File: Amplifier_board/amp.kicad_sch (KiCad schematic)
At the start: 24 parts, among them U1 TPA3111D1PWPR

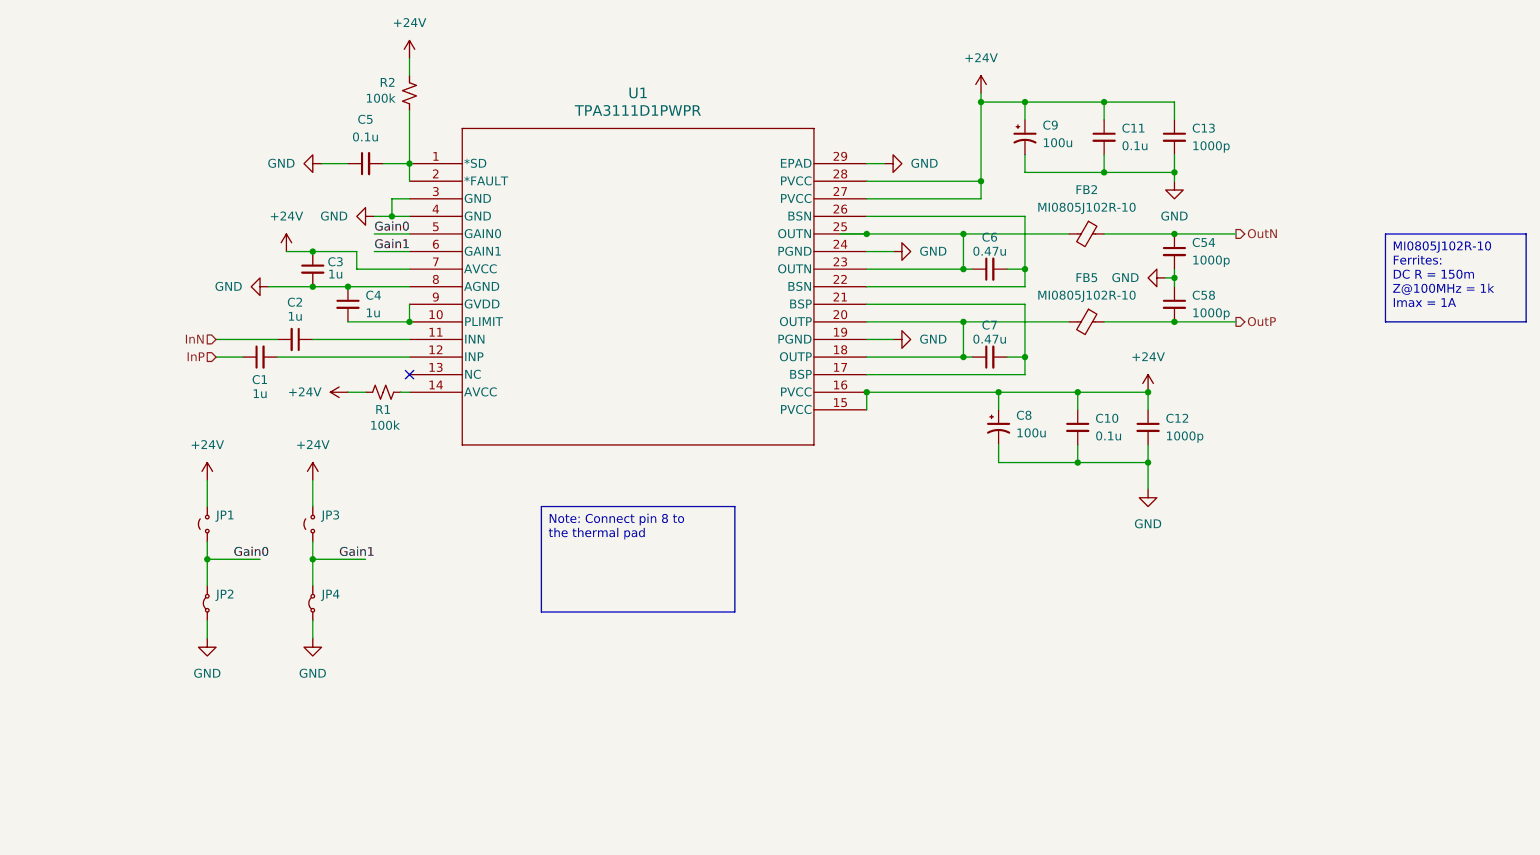
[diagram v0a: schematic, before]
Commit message: Added buffers at DAC outputs
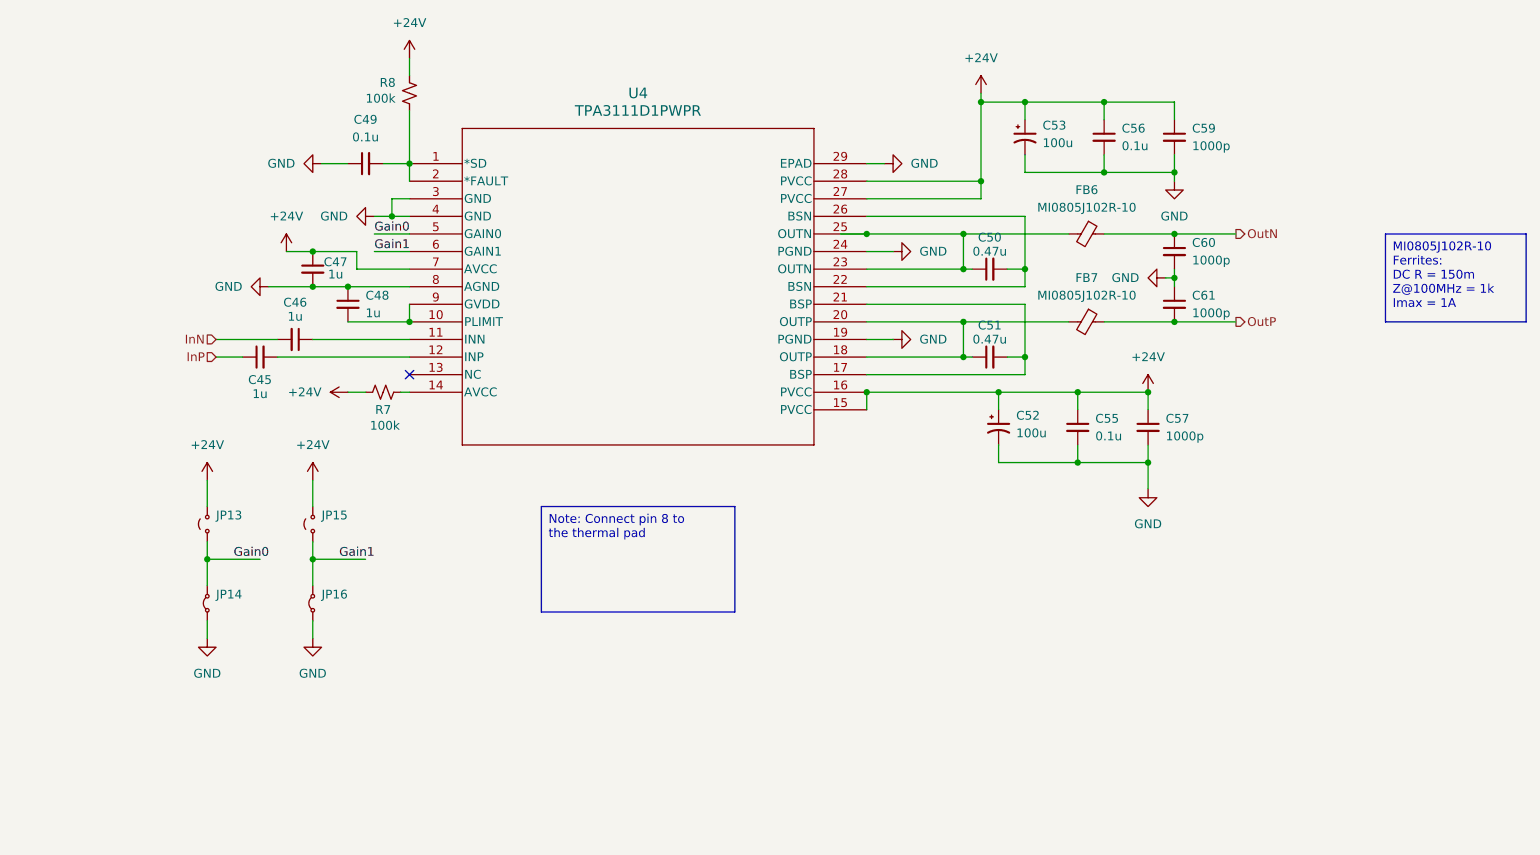
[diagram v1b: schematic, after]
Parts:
- renumbered C1 to C45, C2 to C46, C3 to C47, C4 to C48, C5 to C49, C6 to C50, C7 to C51, C8 to C52, C9 to C53, C10 to C55, C11 to C56, C12 to C57, C13 to C59, C54 to C60, C58 to C61, FB2 to FB6, FB5 to FB7, JP1 to JP13, JP2 to JP14, JP3 to JP15, JP4 to JP16, R1 to R7, R2 to R8, U1 to U4
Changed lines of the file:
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@@
 		(dnp no)
 		(fields_autoplaced yes)
-		(property "Reference" "C4"
+		(property "Reference" "C48"
 			(at 96.52 82.5562 0)
 			(effects
@@
 		(on_board yes)
 		(dnp no)
-		(property "Reference" "C6"
+		(property "Reference" "C50"
 			(at 186.69 74.168 90)
 			(effects
@@
 		(on_board yes)
 		(dnp no)
-		(property "Reference" "R2"
+		(property "Reference" "R8"
 			(at 98.552 51.816 0)
 			(effects
@@
 		(on_board yes)
 		(dnp no)
-		(property "Reference" "C3"
+		(property "Reference" "C47"
 			(at 92.202 77.724 0)
 			(effects
@@
 		(dnp no)
 		(fields_autoplaced yes)
-		(property "Reference" "JP2"
+		(property "Reference" "JP14"
 			(at 74.93 125.7299 90)
 			(effects
@@
 		(dnp no)
 		(fields_autoplaced yes)
-		(property "Reference" "#PWR016"
+		(property "Reference" "#PWR072"
 			(at 209.55 116.84 0)
 			(effects
@@
 		(dnp no)
 		(fields_autoplaced yes)
-		(property "Reference" "#PWR05"
+		(property "Reference" "#PWR060"
 			(at 88.9 113.03 0)
 			(effects
@@
 		(dnp no)
 		(fields_autoplaced yes)
-		(property "Reference" "#PWR015"
+		(property "Reference" "#PWR070"
 			(at 209.55 100.33 0)
 			(effects
@@
 		(dnp no)
 		(fields_autoplaced yes)
-		(property "Reference" "C5"
+		(property "Reference" "C49"
 			(at 96.5263 57.15 90)
 			(effects
@@
 		(dnp no)
 		(fields_autoplaced yes)
-		(property "Reference" "C10"
+		(property "Reference" "C55"
 			(at 201.93 100.3362 0)
 			(effects
@@
 		(dnp no)
 		(fields_autoplaced yes)
-		(property "Reference" "C8"
+		(property "Reference" "C52"
 			(at 190.5 99.8981 0)
 			(effects
@@
 		(dnp no)
 		(fields_autoplaced yes)
-		(property "Reference" "FB2"
+		(property "Reference" "FB6"
 			(at 200.6981 67.31 90)
 			(effects
@@
 					(unit 1)
 				)
+				(path "/991395a4-3885-4774-b551-0bfe029123d3/26541e86-2f42-461f-bb67-92277cc28a80"
+					(reference "FB?")
+					(unit 1)
+				)
 				(path "/991395a4-3885-4774-b551-0bfe029123d3/e8898fe0-55dc-4973-83e9-f265cc01a132"
 					(reference "FB1")
@@
 		(dnp no)
 		(fields_autoplaced yes)
-		(property "Reference" "#PWR02"
+		(property "Reference" "#PWR057"
 			(at 73.66 138.43 0)
 			(effects
@@
 		(dnp no)
 		(fields_autoplaced yes)
-		(property "Reference" "#PWR07"
+		(property "Reference" "#PWR062"
 			(at 83.82 63.5 0)
 			(effects
@@
 		(dnp no)
 		(fields_autoplaced yes)
-		(property "Reference" "C9"
+		(property "Reference" "C53"
 			(at 194.31 57.9881 0)
 			(effects
@@
 		(dnp no)
 		(fields_autoplaced yes)
-		(property "Reference" "JP3"
+		(property "Reference" "JP15"
 			(at 90.17 114.2999 90)
 			(effects
@@
 		(dnp no)
 		(fields_autoplaced yes)
-		(property "Reference" "C13"
+		(property "Reference" "C59"
 			(at 215.9 58.4262 0)
 			(effects
@@
 		(on_board yes)
 		(dnp no)
-		(property "Reference" "C54"
+		(property "Reference" "C60"
 			(at 215.9 74.9362 0)
 			(effects
@@
 		(dnp no)
 		(fields_autoplaced yes)
-		(property "Reference" "U1"
+		(property "Reference" "U4"
 			(at 135.89 53.34 0)
 			(effects
@@
 		(dnp no)
 		(fields_autoplaced yes)
-		(property "Reference" "#PWR03"
+		(property "Reference" "#PWR058"
 			(at 76.2 81.28 0)
 			(effects
@@
 		(dnp no)
 		(fields_autoplaced yes)
-		(property "Reference" "#PWR011"
+		(property "Reference" "#PWR066"
 			(at 177.8 63.5 0)
 			(effects
@@
 		(dnp no)
 		(fields_autoplaced yes)
-		(property "Reference" "C12"
+		(property "Reference" "C57"
 			(at 212.09 100.3362 0)
 			(effects
@@
 		(dnp no)
 		(fields_autoplaced yes)
-		(property "Reference" "#PWR014"
+		(property "Reference" "#PWR069"
 			(at 185.42 57.15 0)
 			(effects
@@
 		(dnp no)
 		(fields_autoplaced yes)
-		(property "Reference" "#PWR017"
+		(property "Reference" "#PWR074"
 			(at 213.36 72.39 0)
 			(effects
@@
 		(dnp no)
 		(fields_autoplaced yes)
-		(property "Reference" "#PWR08"
+		(property "Reference" "#PWR063"
 			(at 97.79 96.52 0)
 			(effects
@@
 		(dnp no)
 		(fields_autoplaced yes)
-		(property "Reference" "#PWR01"
+		(property "Reference" "#PWR056"
 			(at 73.66 113.03 0)
 			(effects
@@
 		(on_board yes)
 		(dnp no)
-		(property "Reference" "R1"
+		(property "Reference" "R7"
 			(at 99.06 99.06 90)
 			(effects
@@
 		(dnp no)
 		(fields_autoplaced yes)
-		(property "Reference" "#PWR010"
+		(property "Reference" "#PWR065"
 			(at 102.87 52.07 0)
 			(effects
@@
 		(dnp no)
 		(fields_autoplaced yes)
-		(property "Reference" "#PWR071"
+		(property "Reference" "#PWR073"
 			(at 205.74 80.01 0)
 			(effects
@@
 		(dnp no)
 		(fields_autoplaced yes)
-		(property "Reference" "C11"
+		(property "Reference" "C56"
 			(at 205.74 58.4262 0)
 			(effects
@@
 		(dnp no)
 		(fields_autoplaced yes)
-		(property "Reference" "FB5"
+		(property "Reference" "FB7"
 			(at 200.6981 80.01 90)
 			(effects
@@
 		(dnp no)
 		(fields_autoplaced yes)
-		(property "Reference" "#PWR013"
+		(property "Reference" "#PWR068"
 			(at 179.07 88.9 0)
 			(effects
@@
 		(on_board yes)
 		(dnp no)
-		(property "Reference" "C2"
+		(property "Reference" "C46"
 			(at 86.36 83.566 90)
 			(effects
@@
 		(dnp no)
 		(fields_autoplaced yes)
-		(property "Reference" "JP1"
+		(property "Reference" "JP13"
 			(at 74.93 114.2999 90)
 			(effects
@@
 		(on_board yes)
 		(dnp no)
-		(property "Reference" "C7"
+		(property "Reference" "C51"
 			(at 186.69 86.868 90)
 			(effects
@@
 		(dnp no)
 		(fields_autoplaced yes)
-		(property "Reference" "#PWR04"
+		(property "Reference" "#PWR059"
 			(at 85.09 80.01 0)
 			(effects
@@
 		(dnp no)
 		(fields_autoplaced yes)
-		(property "Reference" "#PWR012"
+		(property "Reference" "#PWR067"
 			(at 179.07 76.2 0)
 			(effects
@@
 		(dnp no)
 		(fields_autoplaced yes)
-		(property "Reference" "C58"
+		(property "Reference" "C61"
 			(at 215.9 82.5562 0)
 			(effects
@@
 		(dnp no)
 		(fields_autoplaced yes)
-		(property "Reference" "#PWR09"
+		(property "Reference" "#PWR064"
 			(at 91.44 71.12 0)
 			(effects
@@
 		(dnp no)
 		(fields_autoplaced yes)
-		(property "Reference" "#PWR06"
+		(property "Reference" "#PWR061"
 			(at 88.9 138.43 0)
 			(effects
@@
 		(on_board yes)
 		(dnp no)
-		(property "Reference" "C1"
+		(property "Reference" "C45"
 			(at 81.28 94.742 90)
 			(effects
@@
 		(dnp no)
 		(fields_autoplaced yes)
-		(property "Reference" "JP4"
+		(property "Reference" "JP16"
 			(at 90.17 125.7299 90)
 			(effects

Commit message: Added 2.5V regulator circuit, jumpers on buffers
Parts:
- removed FB6, FB7: MI0805J102R-10, symbol Device:FerriteBead_Small
- added L1, L5: 68u, symbol Device:L_Small
- C60, C61: value 1000p -> 0.5u
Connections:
- net OutN: now also L1.2
- net OutP: now also L5.2
- net at C50.1, U4.23 (OUTN), U4.25 (OUTN): now also L1.1
- net at C51.1, U4.18 (OUTP), U4.20 (OUTP): now also L5.1

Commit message: Added footprints for amplifier board
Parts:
- C45, C46, C47, C48, C49, C50, C51, C52, C53, C55, C56, C57, C59, C60, C61: footprint (none) -> Capacitor_SMD:C_0805_2012Metric_Pad1.18x1.45mm_HandSolder
- JP13, JP14, JP15, JP16: footprint (none) -> Jumper:SolderJumper-2_P1.3mm_Open_TrianglePad1.0x1.5mm
- L4: renamed from L1; footprint (none) -> Inductor_SMD:L_Taiyo-Yuden_NR-80xx_HandSoldering
- L8: renamed from L5; footprint (none) -> Inductor_SMD:L_Taiyo-Yuden_NR-80xx_HandSoldering
- R7, R8: footprint (none) -> Resistor_SMD:R_0805_2012Metric_Pad1.20x1.40mm_HandSolder
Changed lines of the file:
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@@
 	)
 	(junction
-		(at 168.91 73.66)
-		(diameter 0)
-		(color 0 0 0 0)
-	)
-	(junction
 		(at 182.88 78.74)
 		(diameter 0)
@@
 	(wire
 		(pts
-			(xy 165.1 73.66) (xy 168.91 73.66)
-		)
-		(stroke
-			(width 0)
-			(type default)
-		)
-	)
-	(wire
-		(pts
 			(xy 168.91 68.58) (xy 185.42 68.58)
 		)
@@
 		)
 	)
-	(text_box "MI0805J102R-10 Ferrites:\nDC R = 150m\nZ@100MHz = 1k\nImax = 1A\n"
-		(exclude_from_sim no)
-		(at 243.84 73.66 0)
-		(size 20.32 12.7)
-		(stroke
-			(width 0)
-			(type default)
-		)
-		(fill
-			(type none)
-		)
-		(effects
-			(font
-				(size 1.27 1.27)
-			)
-			(justify left top)
-		)
-	)
 	(text_box "Note: Connect pin 8 to the thermal pad\n"
 		(exclude_from_sim no)
-		(at 121.92 113.03 0)
+		(at 127 114.3 0)
 		(size 27.94 15.24)
 		(stroke
@@
 			)
 		)
-		(property "Footprint" ""
+		(property "Footprint" "Capacitor_SMD:C_0805_2012Metric_Pad1.18x1.45mm_HandSolder"
 			(at 93.98 83.82 0)
 			(effects
@@
 			)
 		)
-		(property "Footprint" ""
+		(property "Footprint" "Capacitor_SMD:C_0805_2012Metric_Pad1.18x1.45mm_HandSolder"
 			(at 186.69 78.74 0)
 			(effects
@@
 			)
 		)
-		(property "Footprint" ""
+		(property "Footprint" "Resistor_SMD:R_0805_2012Metric_Pad1.20x1.40mm_HandSolder"
 			(at 102.87 53.34 0)
 			(effects
@@
 			)
 		)
-		(property "Footprint" ""
+		(property "Footprint" "Capacitor_SMD:C_0805_2012Metric_Pad1.18x1.45mm_HandSolder"
 			(at 88.9 78.74 0)
 			(effects
@@
 			)
 		)
-		(property "Footprint" ""
+		(property "Footprint" "Jumper:SolderJumper-2_P1.3mm_Open_TrianglePad1.0x1.5mm"
 			(at 73.66 127 0)
 			(effects
@@
 			)
 		)
-		(property "Footprint" ""
+		(property "Footprint" "Capacitor_SMD:C_0805_2012Metric_Pad1.18x1.45mm_HandSolder"
 			(at 96.52 63.5 0)
 			(effects
@@
 			)
 		)
-		(property "Footprint" ""
+		(property "Footprint" "Capacitor_SMD:C_0805_2012Metric_Pad1.18x1.45mm_HandSolder"
 			(at 199.39 101.6 0)
 			(effects
@@
 			)
 		)
-		(property "Footprint" ""
+		(property "Footprint" "Capacitor_SMD:C_0805_2012Metric_Pad1.18x1.45mm_HandSolder"
 			(at 187.96 101.6 0)
 			(effects
@@
 		(dnp no)
 		(fields_autoplaced yes)
-		(property "Reference" "L5"
+		(property "Reference" "L8"
 			(at 200.66 81.28 90)
 			(effects
@@
 			)
 		)
-		(property "Footprint" ""
+		(property "Footprint" "Inductor_SMD:L_Taiyo-Yuden_NR-80xx_HandSoldering"
 			(at 200.66 86.36 0)
 			(effects
@@
 			)
 		)
-		(property "Datasheet" "~"
+		(property "Datasheet" "LSXNH8080YKL680MJG"
 			(at 200.66 86.36 0)
 			(effects
@@
 		(dnp no)
 		(fields_autoplaced yes)
-		(property "Reference" "L1"
+		(property "Reference" "L4"
 			(at 200.66 68.58 90)
 			(effects
@@
 			)
 		)
-		(property "Footprint" ""
+		(property "Footprint" "Inductor_SMD:L_Taiyo-Yuden_NR-80xx_HandSoldering"
 			(at 200.66 73.66 0)
 			(effects
@@
 			)
 		)
-		(property "Footprint" ""
+		(property "Footprint" "Capacitor_SMD:C_0805_2012Metric_Pad1.18x1.45mm_HandSolder"
 			(at 191.77 59.69 0)
 			(effects
@@
 			)
 		)
-		(property "Footprint" ""
+		(property "Footprint" "Jumper:SolderJumper-2_P1.3mm_Open_TrianglePad1.0x1.5mm"
 			(at 88.9 115.57 0)
 			(effects
@@
 			)
 		)
-		(property "Footprint" ""
+		(property "Footprint" "Capacitor_SMD:C_0805_2012Metric_Pad1.18x1.45mm_HandSolder"
 			(at 213.36 59.69 0)
 			(effects
@@
 			)
 		)
-		(property "Footprint" ""
+		(property "Footprint" "Capacitor_SMD:C_0805_2012Metric_Pad1.18x1.45mm_HandSolder"
 			(at 213.36 76.2 0)
 			(effects
@@
 			)
 		)
-		(property "Footprint" ""
+		(property "Footprint" "Capacitor_SMD:C_0805_2012Metric_Pad1.18x1.45mm_HandSolder"
 			(at 209.55 101.6 0)
 			(effects
@@
 			)
 		)
-		(property "Footprint" ""
+		(property "Footprint" "Resistor_SMD:R_0805_2012Metric_Pad1.20x1.40mm_HandSolder"
 			(at 99.06 96.52 0)
 			(effects
@@
 			)
 		)
-		(property "Footprint" ""
+		(property "Footprint" "Capacitor_SMD:C_0805_2012Metric_Pad1.18x1.45mm_HandSolder"
 			(at 203.2 59.69 0)
 			(effects
@@
 			)
 		)
-		(property "Footprint" ""
+		(property "Footprint" "Capacitor_SMD:C_0805_2012Metric_Pad1.18x1.45mm_HandSolder"
 			(at 86.36 88.9 0)
 			(effects
@@
 			)
 		)
-		(property "Footprint" ""
+		(property "Footprint" "Jumper:SolderJumper-2_P1.3mm_Open_TrianglePad1.0x1.5mm"
 			(at 73.66 115.57 0)
 			(effects
@@
 			)
 		)
-		(property "Footprint" ""
+		(property "Footprint" "Capacitor_SMD:C_0805_2012Metric_Pad1.18x1.45mm_HandSolder"
 			(at 186.69 91.44 0)
 			(effects
@@
 			)
 		)
-		(property "Footprint" ""
+		(property "Footprint" "Capacitor_SMD:C_0805_2012Metric_Pad1.18x1.45mm_HandSolder"
 			(at 213.36 83.82 0)
 			(effects
@@
 			)
 		)
-		(property "Footprint" ""
+		(property "Footprint" "Capacitor_SMD:C_0805_2012Metric_Pad1.18x1.45mm_HandSolder"
 			(at 81.28 91.44 0)
 			(effects
@@
 			)
 		)
-		(property "Footprint" ""
+		(property "Footprint" "Jumper:SolderJumper-2_P1.3mm_Open_TrianglePad1.0x1.5mm"
 			(at 88.9 127 0)
 			(effects
